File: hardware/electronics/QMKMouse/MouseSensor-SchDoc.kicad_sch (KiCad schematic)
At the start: 6 parts

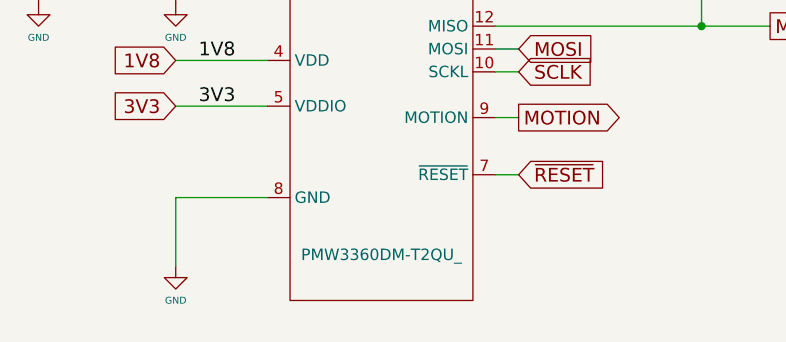
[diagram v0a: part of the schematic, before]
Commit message: update schematic components
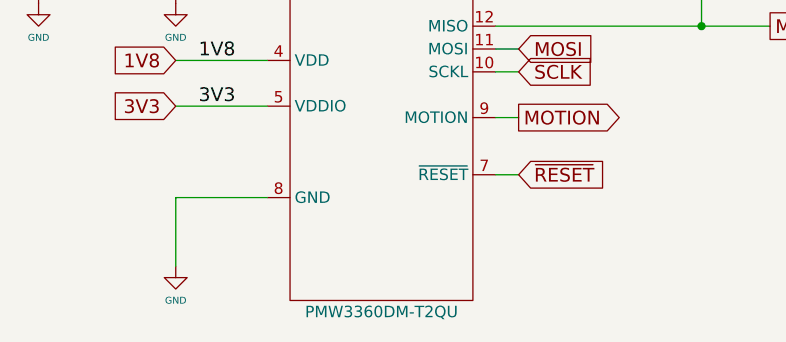
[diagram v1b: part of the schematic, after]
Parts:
- MOS.U.2: value PMW3360DM-T2QU_ -> PMW3360DM-T2QU
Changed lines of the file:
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@@
     (in_bom yes) (on_board yes)
     (property "Reference" "MOS.U.2" (id 0) (at 124.46 85.09 0))
-    (property "Value" "PMW3360DM-T2QU_" (id 1) (at 124.46 125.73 0))
+    (property "Value" "PMW3360DM-T2QU" (id 1) (at 124.46 132.08 0))
     (property "Footprint" "" (id 2) (at 124.46 86.36 0)
       (effects (font (size 1.27 1.27)) hide)

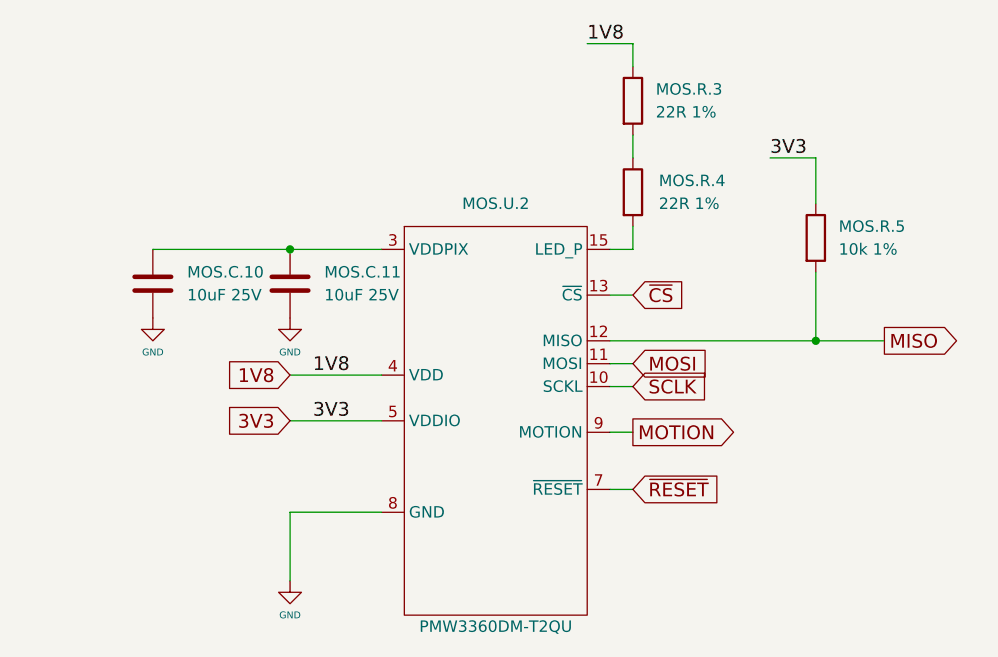
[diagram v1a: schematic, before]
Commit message: update schematic from PCB; sync netlist and fix some symbol orientations; also fix LED symbol
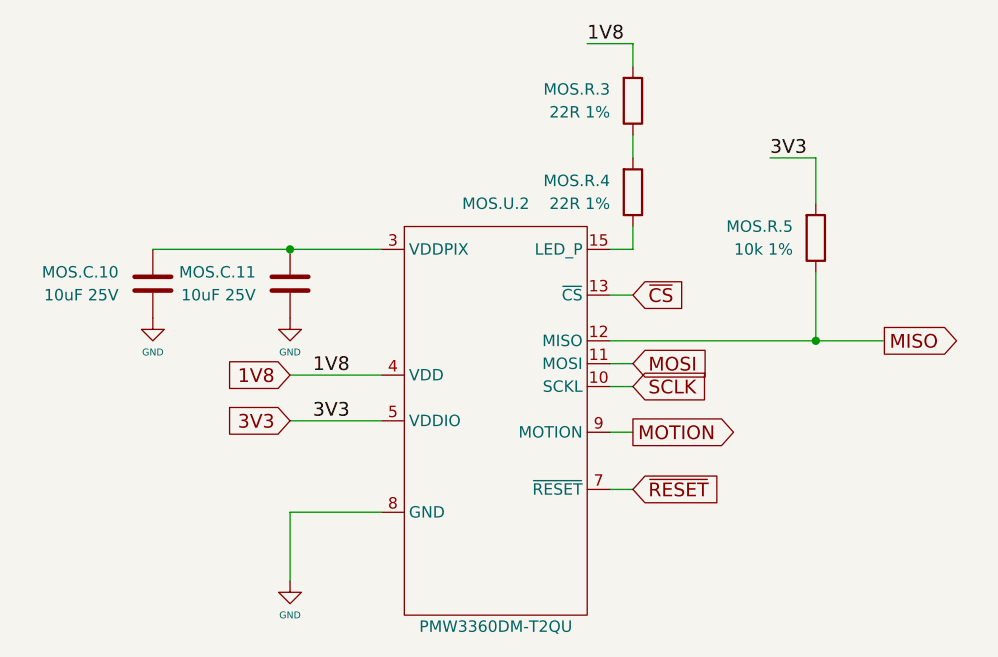
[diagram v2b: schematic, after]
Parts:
- MOS.C.10, MOS.C.11, MOS.R.3, MOS.R.4, MOS.R.5: footprint (none) -> Chip_Passives.PcbLib:0805
- MOS.U.2: footprint (none) -> OptoElectronics.PcbLib:PMW3360DM-T2QU
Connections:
- net 1V8: now also MOS.R.3.2; no longer MOS.R.3.1
- net 3V3: now also MOS.R.5.2; no longer MOS.R.5.1
- net GND: now also MOS.C.10.1, MOS.C.11.1; no longer MOS.C.10.2, MOS.C.11.2
- net MISO: now also MOS.R.5.1; no longer MOS.R.5.2
- net at MOS.R.4.1: now also MOS.U.2.15 (LED_P); no longer MOS.R.3.2
- net at MOS.R.4.2: now also MOS.R.3.1; no longer MOS.U.2.15 (LED_P)
- new net: MOS.C.10.2, MOS.C.11.2, MOS.U.2.3 (VDDPIX)
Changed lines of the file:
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@@
     (pin "1")
   )
-  (symbol (lib_id "Device:R") (at 139.7 83.82 0) (unit 1)
+  (symbol (lib_id "Device:R") (at 139.7 83.82 0) (mirror x) (unit 1)
     (in_bom yes) (on_board yes) (fields_autoplaced)
-    (property "Reference" "MOS.R.4" (id 0) (at 142.5774 82.5499 0)
-      (effects (font (size 1.27 1.27)) (justify left))
+    (property "Reference" "MOS.R.4" (id 0) (at 137.16 82.5499 0)
+      (effects (font (size 1.27 1.27)) (justify right))
     )
-    (property "Value" "22R 1%" (id 1) (at 142.5774 85.0899 0)
-      (effects (font (size 1.27 1.27)) (justify left))
+    (property "Value" "22R 1%" (id 1) (at 137.16 85.0899 0)
+      (effects (font (size 1.27 1.27)) (justify right))
     )
-    (property "Footprint" "" (id 2) (at 137.922 83.82 90)
+    (property "Footprint" "Chip_Passives.PcbLib:0805" (id 2) (at 137.922 83.82 90)
       (effects (font (size 1.27 1.27)) hide)
     )
@@
     (pin "2")
   )
-  (symbol (lib_id "Device:R") (at 160.02 88.9 0) (unit 1)
+  (symbol (lib_id "Device:R") (at 160.02 88.9 0) (mirror x) (unit 1)
     (in_bom yes) (on_board yes) (fields_autoplaced)
-    (property "Reference" "MOS.R.5" (id 0) (at 162.56 87.6299 0)
-      (effects (font (size 1.27 1.27)) (justify left))
+    (property "Reference" "MOS.R.5" (id 0) (at 157.48 87.6299 0)
+      (effects (font (size 1.27 1.27)) (justify right))
     )
-    (property "Value" "10k 1%" (id 1) (at 162.56 90.1699 0)
-      (effects (font (size 1.27 1.27)) (justify left))
+    (property "Value" "10k 1%" (id 1) (at 157.48 90.1699 0)
+      (effects (font (size 1.27 1.27)) (justify right))
     )
-    (property "Footprint" "" (id 2) (at 158.242 88.9 90)
+    (property "Footprint" "Chip_Passives.PcbLib:0805" (id 2) (at 158.242 88.9 90)
       (effects (font (size 1.27 1.27)) hide)
     )
@@
     (pin "2")
   )
-  (symbol (lib_id "Device:C") (at 101.6 93.98 0) (unit 1)
+  (symbol (lib_id "Device:C") (at 101.6 93.98 0) (mirror x) (unit 1)
     (in_bom yes) (on_board yes) (fields_autoplaced)
-    (property "Reference" "MOS.C.11" (id 0) (at 105.41 92.7099 0)
-      (effects (font (size 1.27 1.27)) (justify left))
+    (property "Reference" "MOS.C.11" (id 0) (at 97.79 92.7099 0)
+      (effects (font (size 1.27 1.27)) (justify right))
     )
-    (property "Value" "10uF 25V" (id 1) (at 105.41 95.2499 0)
-      (effects (font (size 1.27 1.27)) (justify left))
+    (property "Value" "10uF 25V" (id 1) (at 97.79 95.2499 0)
+      (effects (font (size 1.27 1.27)) (justify right))
     )
-    (property "Footprint" "" (id 2) (at 102.5652 97.79 0)
+    (property "Footprint" "Chip_Passives.PcbLib:0805" (id 2) (at 102.5652 90.17 0)
       (effects (font (size 1.27 1.27)) hide)
     )
@@
     (property "Reference" "MOS.U.2" (id 0) (at 124.46 85.09 0))
     (property "Value" "PMW3360DM-T2QU" (id 1) (at 124.46 132.08 0))
-    (property "Footprint" "" (id 2) (at 124.46 86.36 0)
+    (property "Footprint" "OptoElectronics.PcbLib:PMW3360DM-T2QU" (id 2) (at 124.46 86.36 0)
       (effects (font (size 1.27 1.27)) hide)
     )
@@
     (pin "9")
   )
-  (symbol (lib_id "Device:C") (at 86.36 93.98 0) (unit 1)
+  (symbol (lib_id "Device:C") (at 86.36 93.98 0) (mirror x) (unit 1)
     (in_bom yes) (on_board yes) (fields_autoplaced)
-    (property "Reference" "MOS.C.10" (id 0) (at 90.17 92.7099 0)
-      (effects (font (size 1.27 1.27)) (justify left))
+    (property "Reference" "MOS.C.10" (id 0) (at 82.55 92.7099 0)
+      (effects (font (size 1.27 1.27)) (justify right))
     )
-    (property "Value" "10uF 25V" (id 1) (at 90.17 95.2499 0)
-      (effects (font (size 1.27 1.27)) (justify left))
+    (property "Value" "10uF 25V" (id 1) (at 82.55 95.2499 0)
+      (effects (font (size 1.27 1.27)) (justify right))
     )
-    (property "Footprint" "" (id 2) (at 87.3252 97.79 0)
+    (property "Footprint" "Chip_Passives.PcbLib:0805" (id 2) (at 87.3252 90.17 0)
       (effects (font (size 1.27 1.27)) hide)
     )
@@
     (pin "2")
   )
-  (symbol (lib_id "Device:R") (at 139.7 73.66 0) (unit 1)
+  (symbol (lib_id "Device:R") (at 139.7 73.66 0) (mirror x) (unit 1)
     (in_bom yes) (on_board yes) (fields_autoplaced)
-    (property "Reference" "MOS.R.3" (id 0) (at 142.24 72.3899 0)
-      (effects (font (size 1.27 1.27)) (justify left))
+    (property "Reference" "MOS.R.3" (id 0) (at 137.16 72.3899 0)
+      (effects (font (size 1.27 1.27)) (justify right))
     )
-    (property "Value" "22R 1%" (id 1) (at 142.24 74.9299 0)
-      (effects (font (size 1.27 1.27)) (justify left))
+    (property "Value" "22R 1%" (id 1) (at 137.16 74.9299 0)
+      (effects (font (size 1.27 1.27)) (justify right))
     )
-    (property "Footprint" "" (id 2) (at 137.922 73.66 90)
+    (property "Footprint" "Chip_Passives.PcbLib:0805" (id 2) (at 137.922 73.66 90)
       (effects (font (size 1.27 1.27)) hide)
     )
